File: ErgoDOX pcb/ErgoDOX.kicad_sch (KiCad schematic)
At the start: 64 parts, among them J1 USB, J2 3.5mm, J3 JMP, J4 JMP, SW0:10 SW0:3, SW0:11 SW0:2, SW0:12 SW0:1, SW0:7 SW0:6, SW0:8 SW0:5, SW0:9 SW0:4, SW1:10 SW1:3, SW1:11 SW1:2, SW1:12 SW1:1, SW1:13 SW1:0, SW1:9 SW1:4, SW2:10 SW2:3, SW2:11 SW2:2, SW2:12 SW2:1, SW2:13 SW2:0, SW2:7 SW2:6, SW2:8 SW2:5, SW2:9 SW2:4, SW3:10 SW3:3, SW3:11 SW3:2, SW3:12 SW3:1, SW3:13 SW3:0, SW3:8 SW3:5, SW3:9 SW3:4, SW4:10 SW4:3, SW4:11 SW4:2, SW4:12 SW4:1, SW4:13 SW4:0, SW4:7 SW4:6, SW4:8 SW4:5, SW4:9 SW4:4, SW5:10 SW5:3, SW5:11 SW5:2, SW5:12 SW5:1, SW5:13 SW5:0, SW5:7 SW5:6, SW5:8 SW5:5, SW5:9 SW5:4, U1 TinyS3_Symbol, U2 MCP23018

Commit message: Add two-handed ESP32-S3 boards
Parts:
- removed SW_RST1: SWITCH_PUSH, Buttons_Switches_SMD:SW_SPST_B3U-1000P, symbol component:SWITCH_PUSH
- removed U1: TinyS3_Symbol, Espressif:TinyS3, symbol TinyS3:TinyS3_Symbol
- removed U2: MCP23018, symbol component:MCP23018
- added C? (x4): 0.1uF, symbol pspice:CAP
- added C? (x3): 10uF, symbol pspice:CAP
- added D? (x3): ESD9B3.3ST5G, Diode_SMD:D_SOD-923, symbol Diode:ESD9B3.3ST5G
- added D?: 1N5819, Diode_THT:D_DO-41_SOD81_P10.16mm_Horizontal, symbol Diode:1N5819
- added J?: JTAG, symbol component:6PIN
- added J?: USB_C_Receptacle_USB2.0, symbol Connector:USB_C_Receptacle_USB2.0
- added J?: PROG, symbol component:6PIN
- added R? (x2): 5.1k, Resistor_SMD:R_0805_2012Metric_Pad1.20x1.40mm_HandSolder, symbol Device:R
- added R? (x2): 0, symbol component:RESISTOR
- added SW_RST? (x2): SWITCH_PUSH, Buttons_Switches_SMD:SW_SPST_B3U-1000P, symbol component:SWITCH_PUSH
- added U?: LM337_SOT223, Package_TO_SOT_SMD:SOT-223-3_TabPin2, symbol Regulator_Linear:LM337_SOT223
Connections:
- net GND: now also C?.1, C?.1, C?.2, C?.2, C?.2, C?.2, C?.2, D?.1 (A1), D?.1 (A1), D?.1 (A1), J?.2, J?.4, J?.A1 (GND), J?.A12 (GND), J?.B1 (GND), J?.B12 (GND), R?.1, R?.1, SW_RST?.0 (GND), SW_RST?.0 (GND), SW_RST?.2, SW_RST?.2, U?.1 (ADJ)
- net VCC: now also C?.1, C?.1, J?.1, J?.2, U?.3 (VO)
- net SCLM renamed esp_lh/SCLM
- net SDAM renamed esp_lh/SDAM
- new net: D?.2 (A), D?.2 (A2), J?.A4 (VBUS), J?.A9 (VBUS), J?.B4 (VBUS), J?.B9 (VBUS)
- new net: J?.A5 (CC1), R?.2
- new net: J?.B5 (CC2), R?.2
- new net: C?.2, R?.1, SW_RST?.1 (x2)
- new net BOOT: J?.6, R?.2
- new net D+: D?.2 (A2), J?.A6 (D+), J?.B6 (D+)
- new net D-: D?.2 (A2), J?.A7 (D-), J?.B7 (D-)
- new net EN: J?.1, R?.2
- new net TCK: J?.6
- new net TDI: J?.4
- new net TDO: J?.5
- new net TMS: J?.3
- new net U0RXD: J?.5
- new net U0TXD: J?.3
- new net VCC_5V: C?.1, C?.1, C?.1, D?.1 (K), U?.2 (VI)
- no-connect marks 11 -> 5
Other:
- added sheet esp_lh (esp_lh.kicad_sch)
- added sheet esp_rh (esp_rh.kicad_sch)

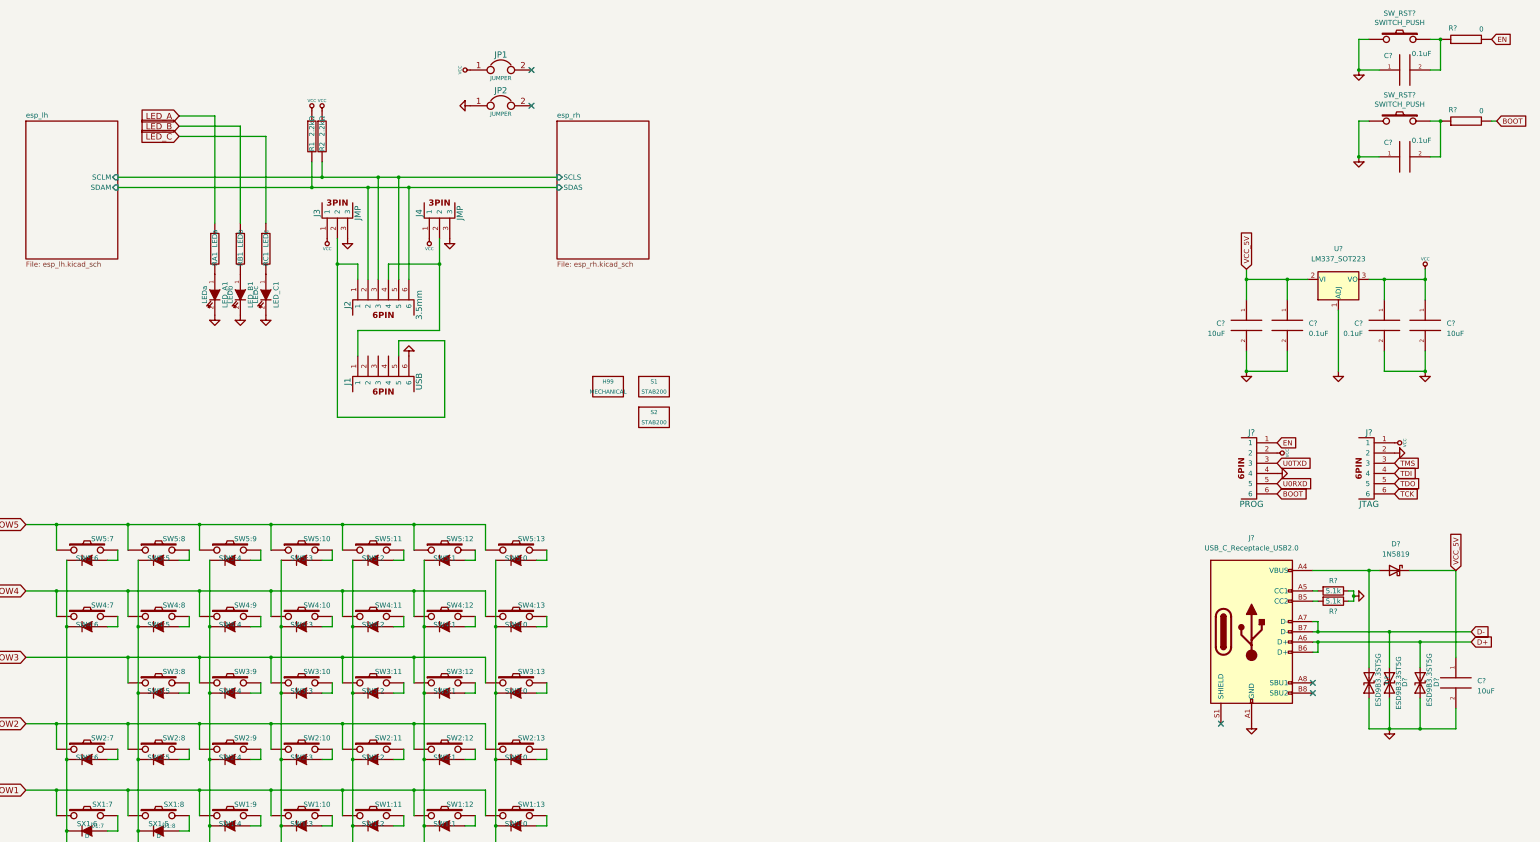
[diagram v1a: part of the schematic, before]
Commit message: Create preliminary layout
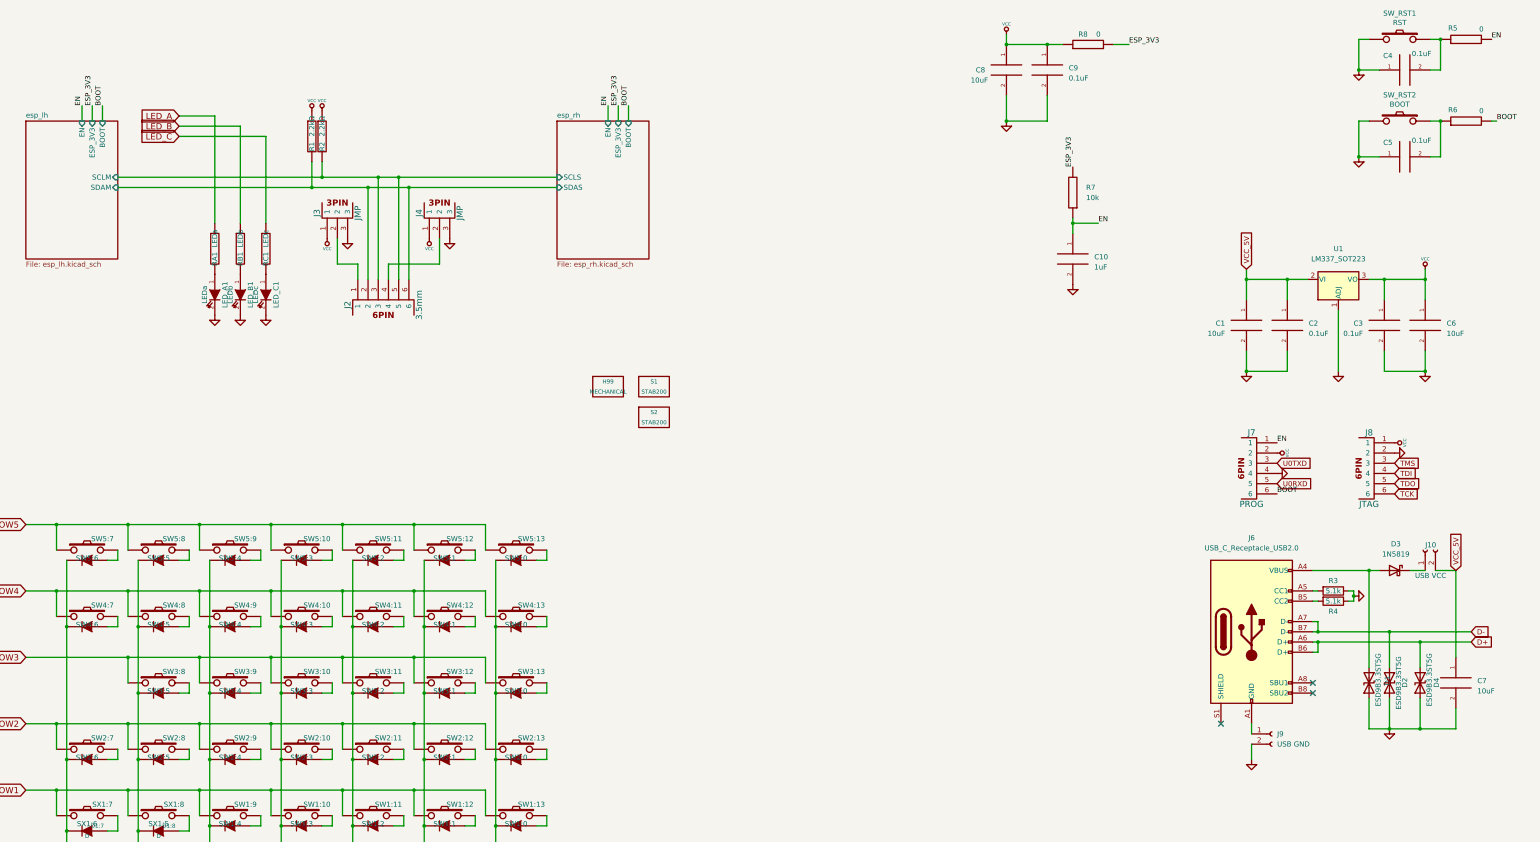
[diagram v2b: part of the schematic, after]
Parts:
- removed J1: USB, symbol component:6PIN
- removed JP1, JP2: JUMPER, symbol component:JUMPER
- added C10: 1uF, Capacitor_THT:C_Disc_D5.0mm_W2.5mm_P5.00mm, symbol pspice:CAP
- added C8: 10uF, Capacitor_THT:C_Disc_D5.0mm_W2.5mm_P5.00mm, symbol pspice:CAP
- added C9: 0.1uF, Capacitor_THT:C_Disc_D5.0mm_W2.5mm_P5.00mm, symbol pspice:CAP
- added J10: USB VCC, Connector_PinHeader_2.54mm:PinHeader_1x02_P2.54mm_Vertical, symbol Connector:Conn_01x02_Female
- added J9: USB GND, Connector_PinHeader_2.54mm:PinHeader_1x02_P2.54mm_Vertical, symbol Connector:Conn_01x02_Female
- added R7: 10k, Resistor_THT:R_Axial_DIN0207_L6.3mm_D2.5mm_P7.62mm_Horizontal, symbol component:RESISTOR
- added R8: 0, Resistor_SMD:R_0805_2012Metric_Pad1.20x1.40mm_HandSolder, symbol component:RESISTOR
- C1, C2, C3, C4, C5, C6, C7: renamed from C?; footprint (none) -> Capacitor_THT:C_Disc_D5.0mm_W2.5mm_P5.00mm
- J6: renamed from J?; footprint (none) -> Connector_USB:USB_C_Receptacle_GCT_USB4085
- J7, J8: renamed from J?; footprint (none) -> Connector_PinHeader_2.54mm:PinHeader_2x03_P2.54mm_Vertical
- R1, R2, RA1, RB1, RC1: footprint (none) -> Resistor_THT:R_Axial_DIN0207_L6.3mm_D2.5mm_P7.62mm_Horizontal
- R3, R4: renamed from R?; footprint Resistor_SMD:R_0805_2012Metric_Pad1.20x1.40mm_HandSolder -> Resistor_THT:R_Axial_DIN0207_L6.3mm_D2.5mm_P7.62mm_Horizontal
- R5, R6: renamed from R?; footprint (none) -> Resistor_SMD:R_0805_2012Metric_Pad1.20x1.40mm_HandSolder
- SW_RST1: renamed from SW_RST?; value SWITCH_PUSH -> RST
- SW_RST2: renamed from SW_RST?; value SWITCH_PUSH -> BOOT
- gave numbers to parts that had none: 5
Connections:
- net EN: now also C10.1, R7.1
- net GND: now also C10.2, C8.2, C9.2, J9.2 (Pin_2); no longer J6.A1 (GND), J6.A12 (GND), J6.B1 (GND), J6.B12 (GND)
- net VCC: now also C8.1, C9.1, R8.1
- net VCC_5V: now also J10.2 (Pin_2); no longer D3.1 (K)
- new net: J6.A1 (GND), J6.A12 (GND), J6.B1 (GND), J6.B12 (GND), J9.1 (Pin_1)
- new net: D3.1 (K), J10.1 (Pin_1)
- new net ESP_3V3: R7.2, R8.2
- no-connect marks 5 -> 3
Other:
- sheet esp_lh ports: added BOOT, EN, ESP_3V3; removed none
- sheet esp_rh ports: added BOOT, EN, ESP_3V3; removed none

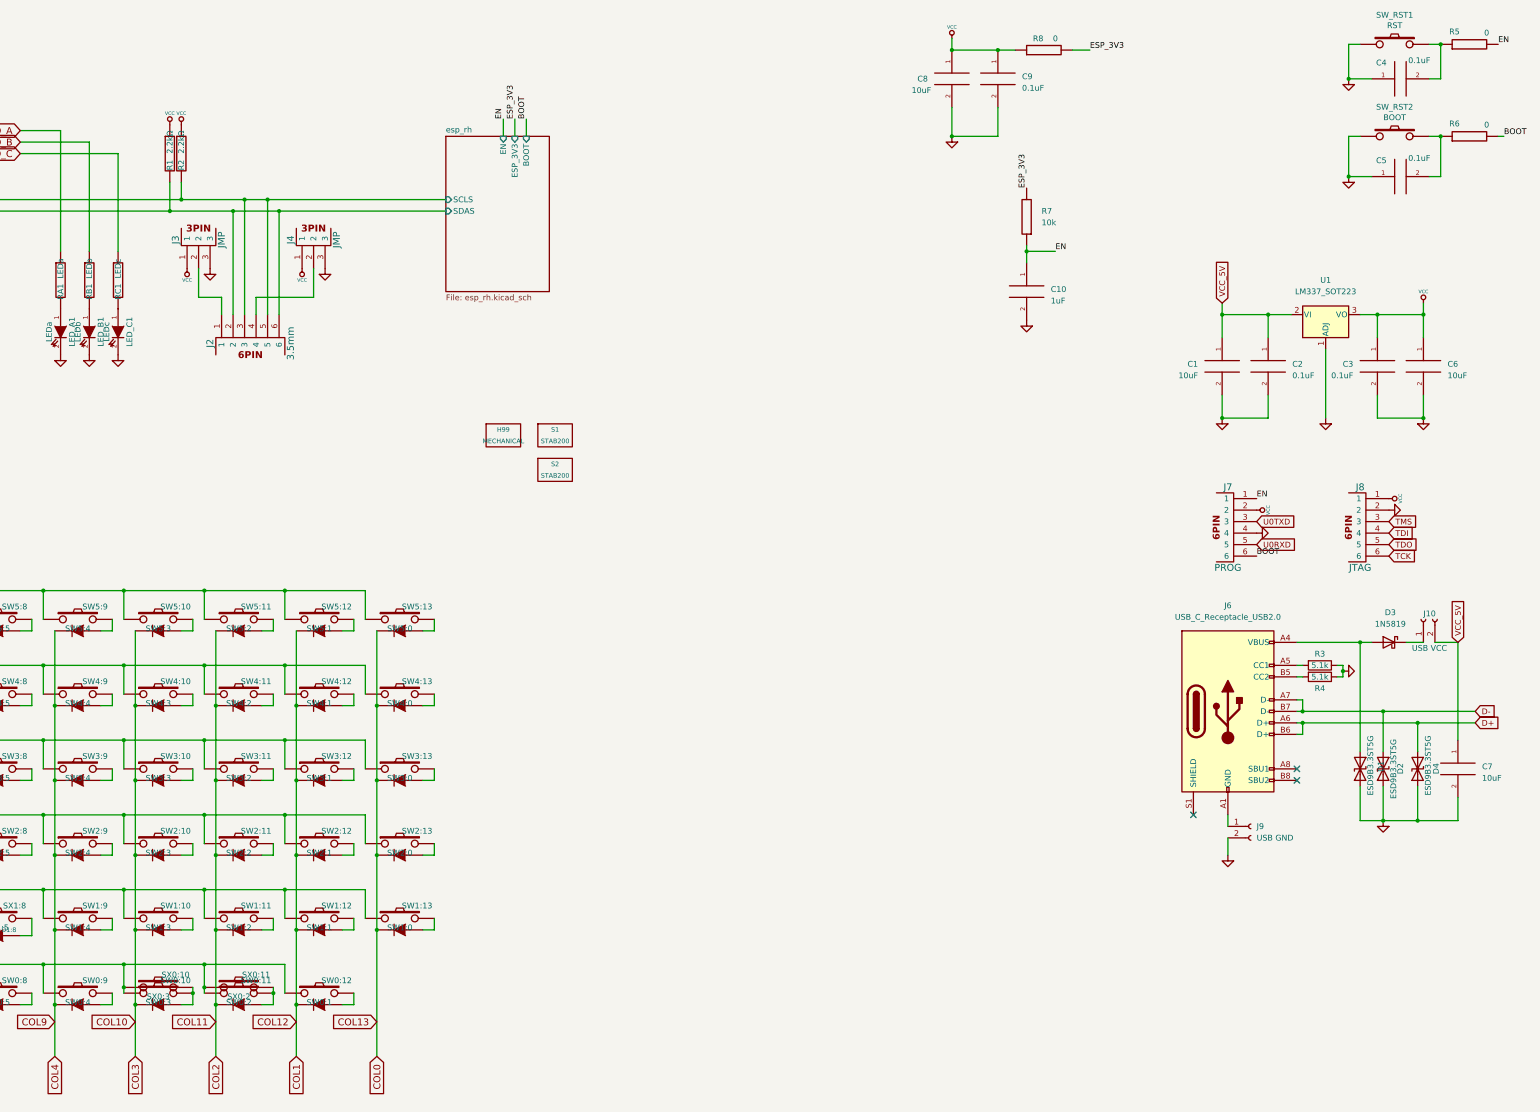
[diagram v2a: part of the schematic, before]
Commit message: Place components in more final layout
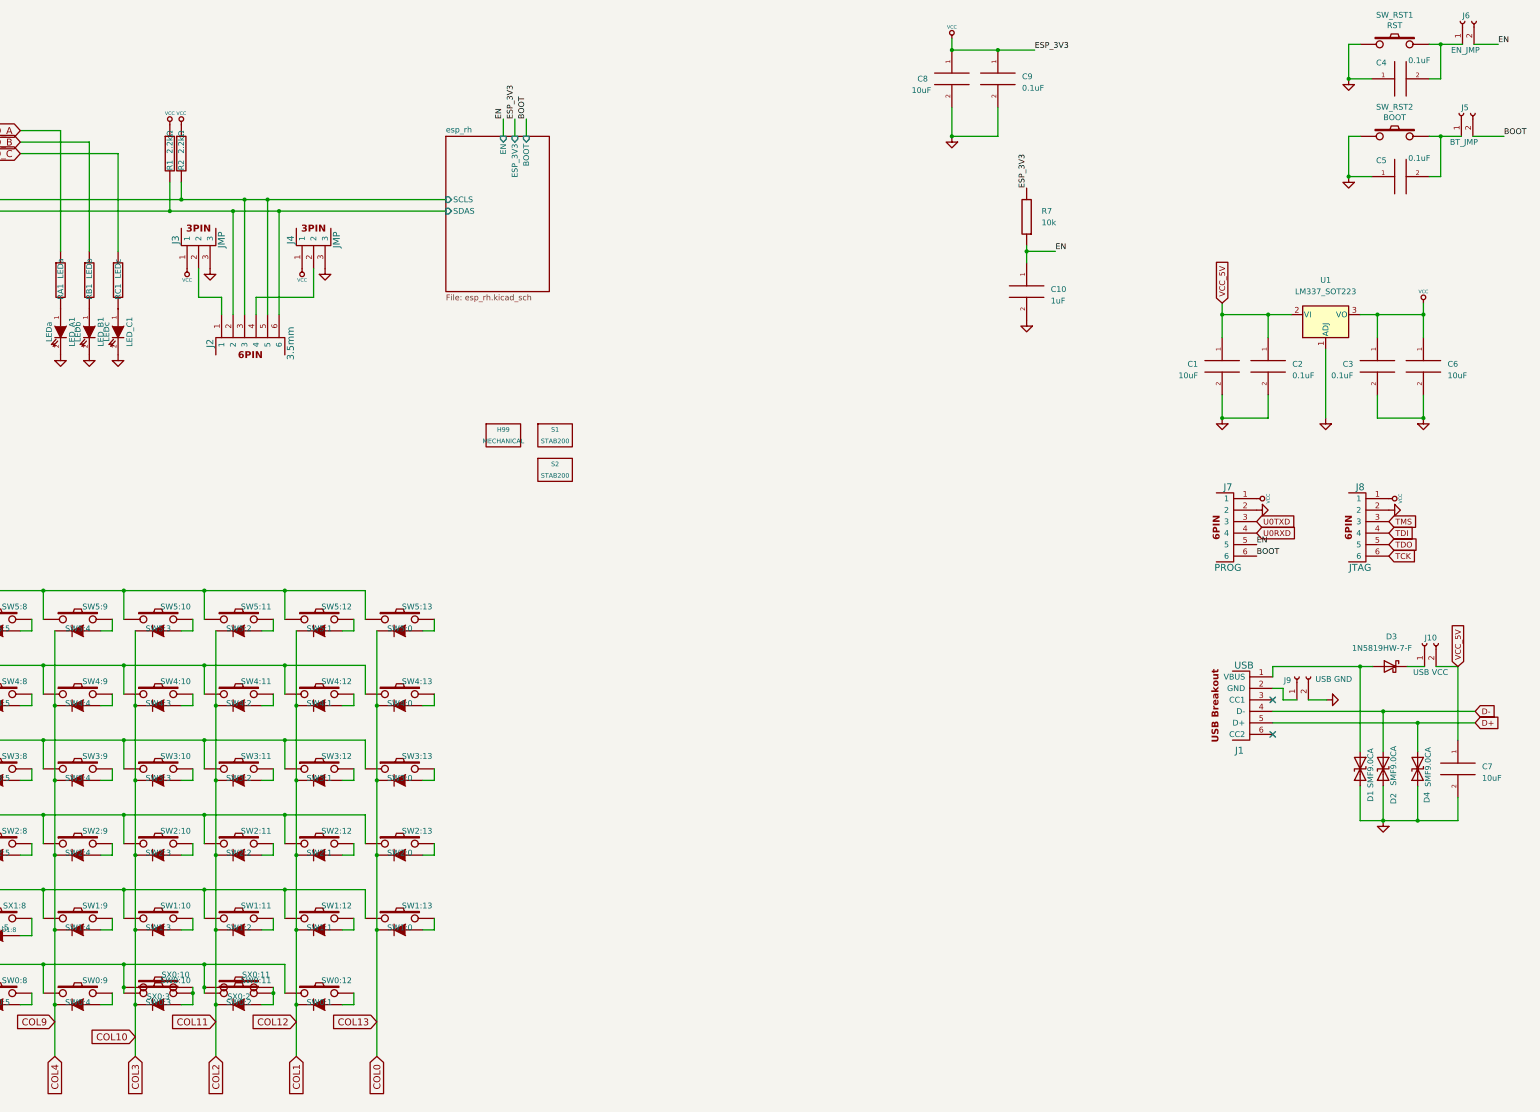
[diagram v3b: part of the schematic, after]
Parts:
- removed J6: USB_C_Receptacle_USB2.0, Connector_USB:USB_C_Receptacle_GCT_USB4085, symbol Connector:USB_C_Receptacle_USB2.0
- removed R3, R4: 5.1k, Resistor_THT:R_Axial_DIN0207_L6.3mm_D2.5mm_P7.62mm_Horizontal, symbol Device:R
- removed R5, R6, R8: 0, Resistor_SMD:R_0805_2012Metric_Pad1.20x1.40mm_HandSolder, symbol component:RESISTOR
- added J1: USB, ErgoDOX pcb:SF USB-C Breakout, symbol component:6PIN
- added J5: BT_JMP, Connector_PinHeader_2.54mm:PinHeader_1x02_P2.54mm_Vertical, symbol Connector:Conn_01x02_Female
- added J6: EN_JMP, Connector_PinHeader_2.54mm:PinHeader_1x02_P2.54mm_Vertical, symbol Connector:Conn_01x02_Female
- D1, D2, D4: value ESD9B3.3ST5G -> SMF9.0CA; footprint Diode_SMD:D_SOD-923 -> Diode_SMD:D_SOD-123
- D3: value 1N5819 -> 1N5819HW-7-F; footprint Diode_THT:D_DO-41_SOD81_P10.16mm_Horizontal -> Diode_SMD:D_SOD-123
- J7, J8: footprint Connector_PinHeader_2.54mm:PinHeader_2x03_P2.54mm_Vertical -> Connector_PinHeader_2.54mm:PinHeader_1x06_P2.54mm_Vertical
- SW_RST1, SW_RST2: footprint Buttons_Switches_SMD:SW_SPST_B3U-1000P -> Button_Switch_SMD:SW_SPST_B3U-1000P
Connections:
- net ESP_3V3 is gone; now on net VCC: R7.2
- net BOOT: now also J5.2 (Pin_2)
- net D+: now also J1.5 (D+)
- net D-: now also J1.4 (D-)
- net EN: now also J7.5, J6.2 (Pin_2); no longer J7.1
- net GND: now also J7.2; no longer J7.4
- net U0RXD: now also J7.4; no longer J7.5
- net VCC: now also J7.1; no longer J7.2
- net at D1.2 (A2), D3.2 (A): now also J1.1 (VBUS)
- net at J9.1 (Pin_1): now also J1.2 (GND)
- net at C4.2, SW_RST1.1: now also J6.1 (Pin_1)
- net at C5.2, SW_RST2.1: now also J5.1 (Pin_1)
- no-connect marks 3 -> 2
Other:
- moved on the sheet: D3, J10, J9
